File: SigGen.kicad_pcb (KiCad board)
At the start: 2 copper layers, 87 x 46 mm, 4 parts, among them M1 HC-SR08-AD9851, U1 ILI9341_SPI_Touch_SD

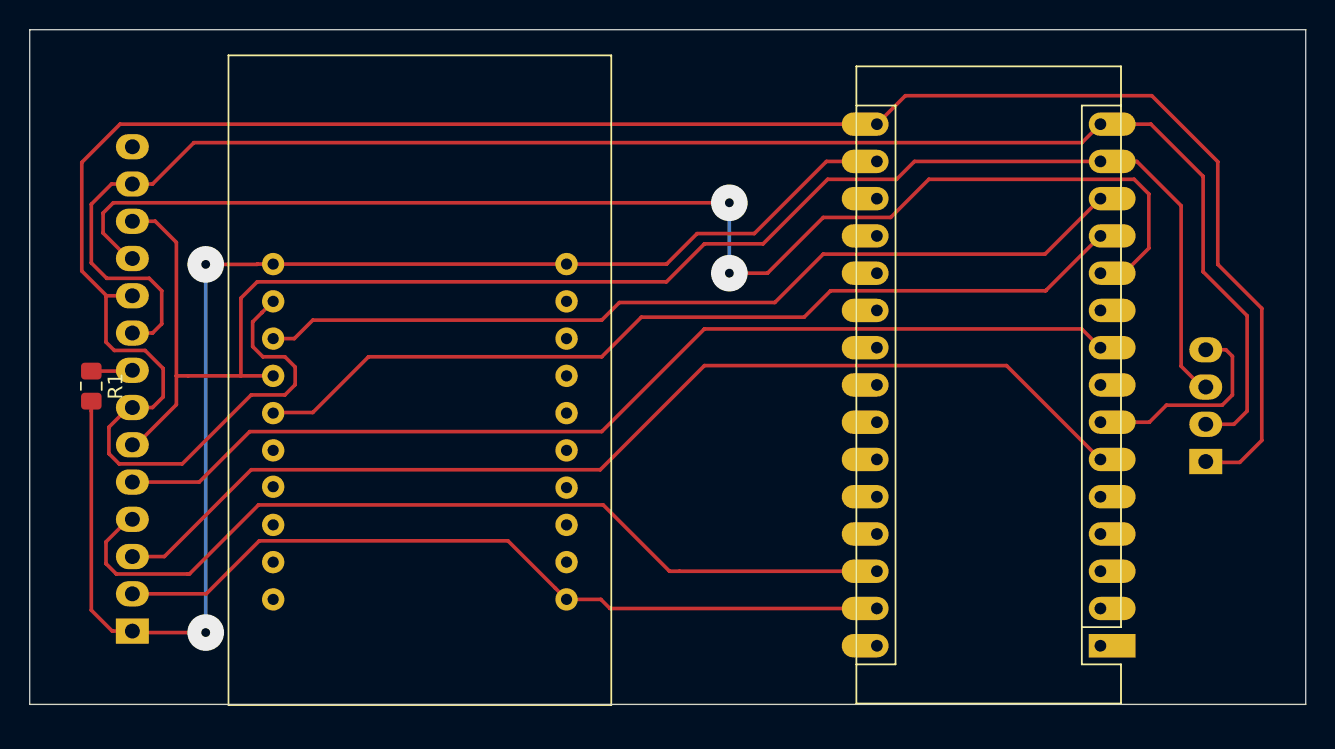
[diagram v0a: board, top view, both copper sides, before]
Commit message: Added test points for external wiring
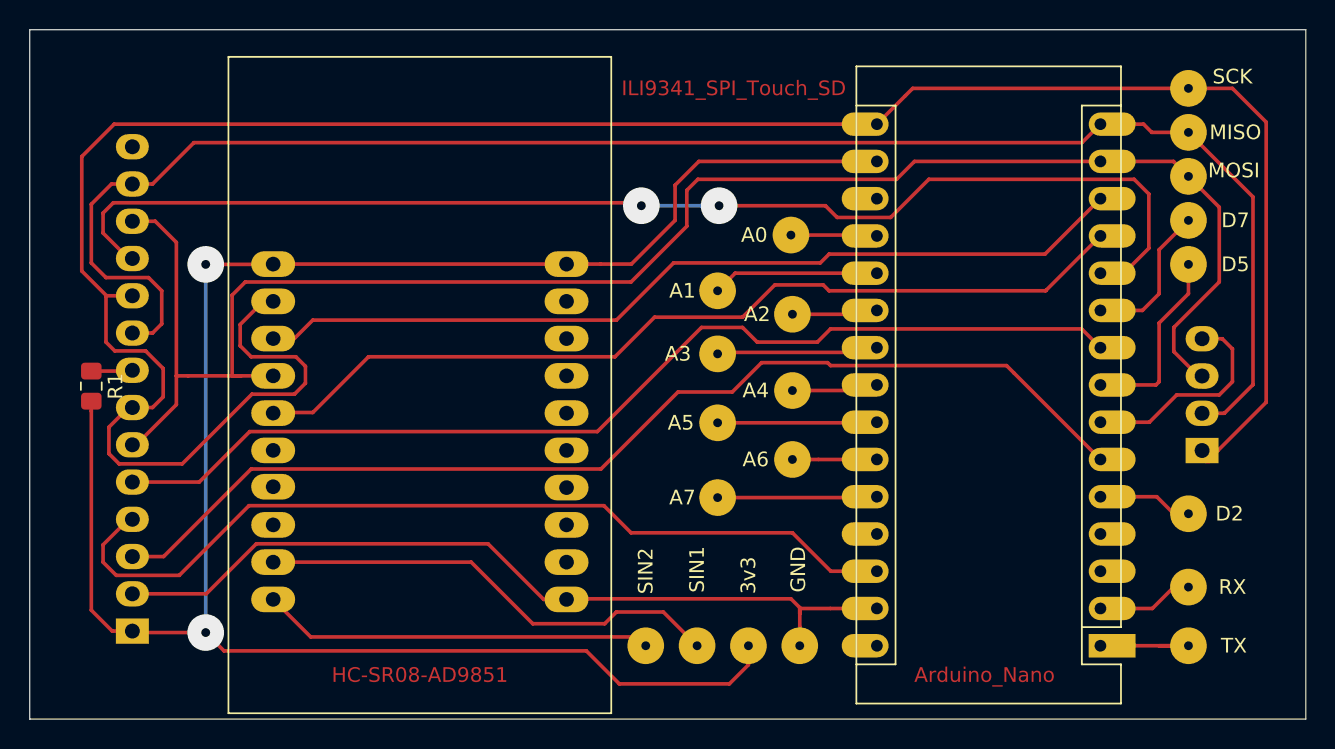
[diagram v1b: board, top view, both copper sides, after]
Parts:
- added 3v3: TestPoint, SigGen:Testpoint, F.Cu at (109.0, 74.0)
- added A0: TestPoint, SigGen:Testpoint, F.Cu at (111.9, 46.0)
- added A1: TestPoint, SigGen:Testpoint, F.Cu at (106.9, 49.8)
- added A2: TestPoint, SigGen:Testpoint, F.Cu at (112.0, 51.4)
- added A3: TestPoint, SigGen:Testpoint, F.Cu at (106.9, 54.1)
- added A4: TestPoint, SigGen:Testpoint, F.Cu at (112.0, 56.6)
- added A5: TestPoint, SigGen:Testpoint, F.Cu at (106.9, 58.8)
- added A6: TestPoint, SigGen:Testpoint, F.Cu at (112.0, 61.3)
- added A7: TestPoint, SigGen:Testpoint, F.Cu at (106.9, 63.9)
- added D2: TestPoint, SigGen:Testpoint, F.Cu at (139.0, 65.0)
- added D5: TestPoint, SigGen:Testpoint, F.Cu at (139.0, 48.0)
- added D7: TestPoint, SigGen:Testpoint, F.Cu at (139.0, 45.0)
- added GND: TestPoint, SigGen:Testpoint, F.Cu at (112.5, 74.0)
- added MISO: TestPoint, SigGen:Testpoint, F.Cu at (139.0, 39.0)
- added MOSI: TestPoint, SigGen:Testpoint, F.Cu at (139.0, 42.0)
- added RX: TestPoint, SigGen:Testpoint, F.Cu at (139.0, 70.0)
- added SCK: TestPoint, SigGen:Testpoint, F.Cu at (139.0, 36.0)
- added SIN1: TestPoint, SigGen:Testpoint, F.Cu at (105.5, 74.0)
- added SIN2: TestPoint, SigGen:Testpoint, F.Cu at (102.0, 74.0)
- added TX: TestPoint, SigGen:Testpoint, F.Cu at (139.0, 74.0)
- Ard1: renamed from A1; value Arduino_Nano_v3.x -> Arduino_Nano
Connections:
- net /MISO renamed Net-(Ard1-Pad15)
- net /MOSI renamed Net-(Ard1-Pad14)
- net /SCK renamed Net-(Ard1-Pad16)
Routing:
- net /3v3: track 97.3 -> 139.0 mm
- net Net-(M1-Pad19): track 0.00 -> 33.0 mm
- net Net-(M1-Pad20): track 0.00 -> 26.7 mm
- net Net-(Ard1-Pad8): track 0.00 -> 14.7 mm
- net Net-(A1-Pad1): track 0.00 -> 11.4 mm
- net Net-(A3-Pad1): track 0.00 -> 11.0 mm
- net Net-(A7-Pad1): track 0.00 -> 10.9 mm
- net Net-(A5-Pad1): track 0.00 -> 10.9 mm
- net Net-(Ard1-Pad10): track 0.00 -> 10.3 mm
- net Net-(Ard1-Pad1): track 0.00 -> 7.00 mm
- net Net-(Ard1-Pad16): track 157.1 -> 164.0 mm
- net Net-(Ard1-Pad5): track 0.00 -> 6.48 mm
- net Net-(Ard1-Pad14): track 113.1 -> 119.3 mm
- net Net-(A4-Pad1): track 0.00 -> 5.92 mm
- net Net-(A0-Pad1): track 0.00 -> 5.88 mm
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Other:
- board size 87 x 46 mm -> 87 x 47 mm

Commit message: Updated with ground fills
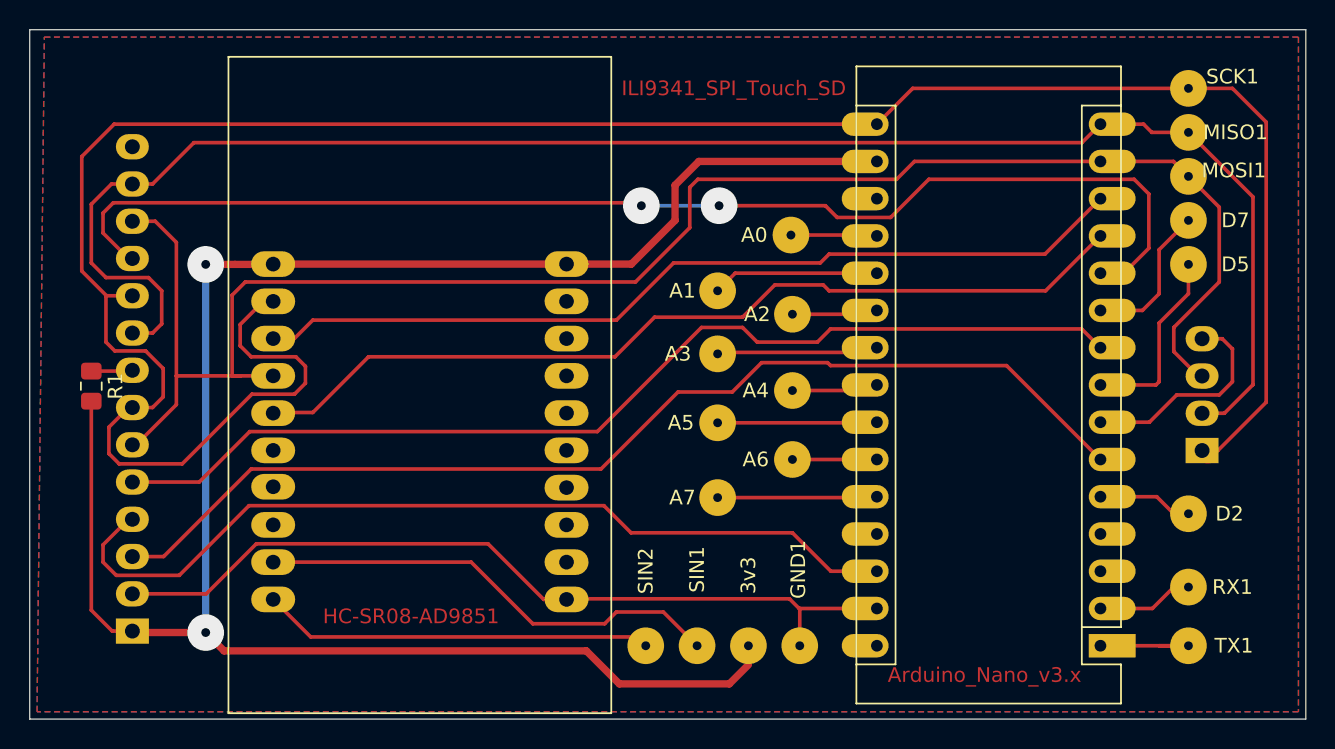
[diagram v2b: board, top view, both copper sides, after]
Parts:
- Ard1: value Arduino_Nano -> Arduino_Nano_v3.x
- renumbered GND to GND1, MISO to MISO1, MOSI to MOSI1, RX to RX1, SCK to SCK1, TX to TX1
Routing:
- net /3v3: track 139.0 -> 141.6 mm
- net /GND: track 57.9 -> 56.6 mm
- added copper zone on B.Cu, net /GND
- added copper zone on F.Cu, net /GND
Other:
- net class PWR added: clearance 0.2, trace_width 0.5, via_dia 1, via_drill 0.6

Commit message: Track size increased to 0.4mm
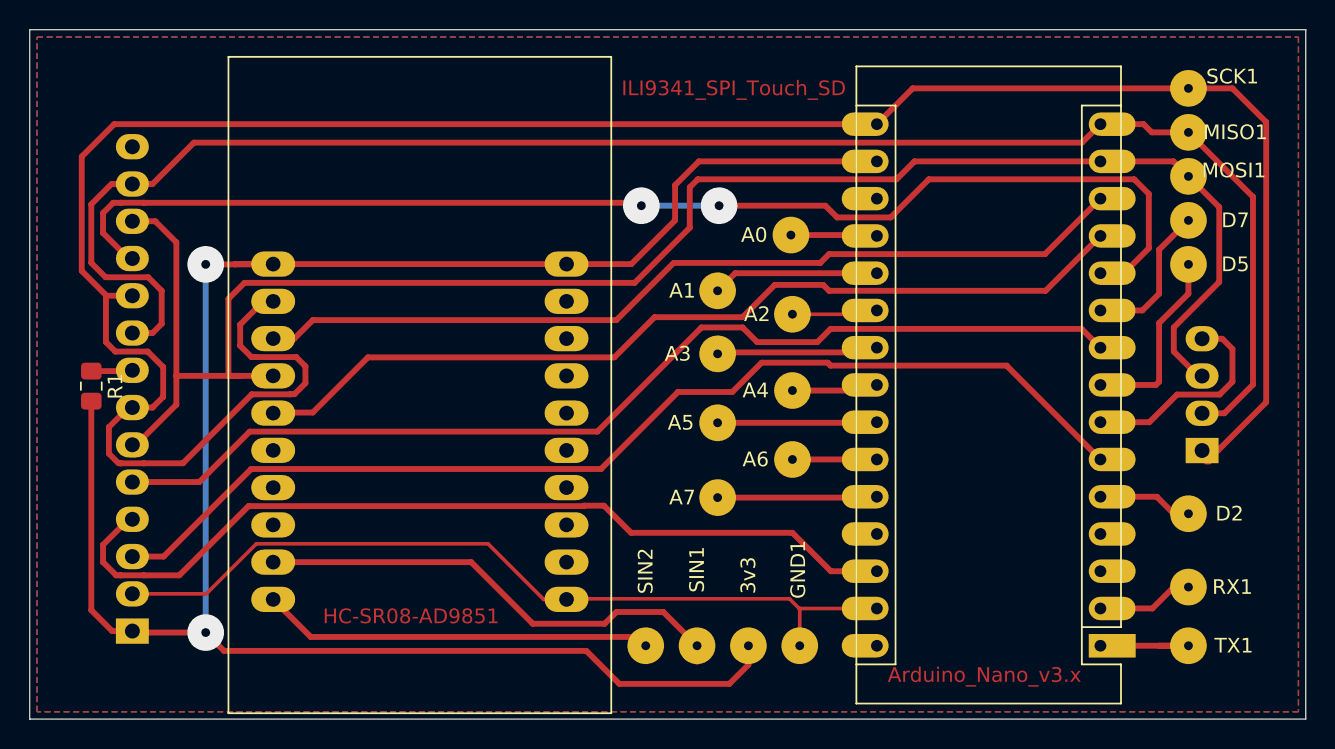
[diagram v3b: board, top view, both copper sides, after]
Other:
- net class Default: trace_width 0.25 -> 0.4
- net class Thread added: clearance 0.2, trace_width 0.25, via_dia 1, via_drill 0.6
